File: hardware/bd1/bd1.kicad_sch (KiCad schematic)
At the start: 61 parts, among them J1 Conn_02x03_Odd_Even, U1 STM32L412CBTx

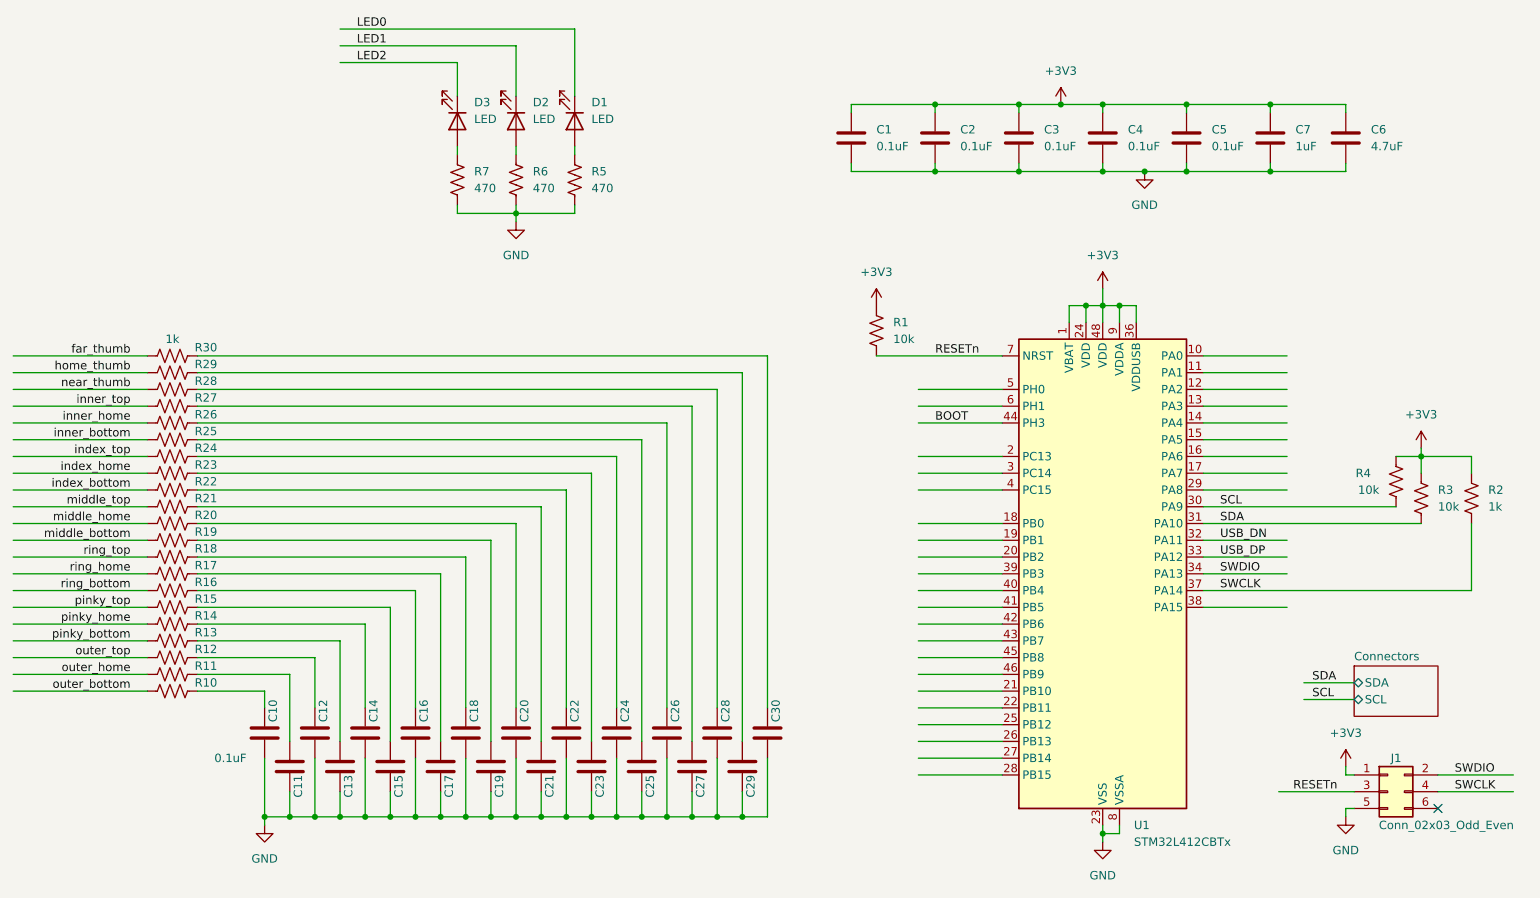
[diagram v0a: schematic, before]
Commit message: USB routing
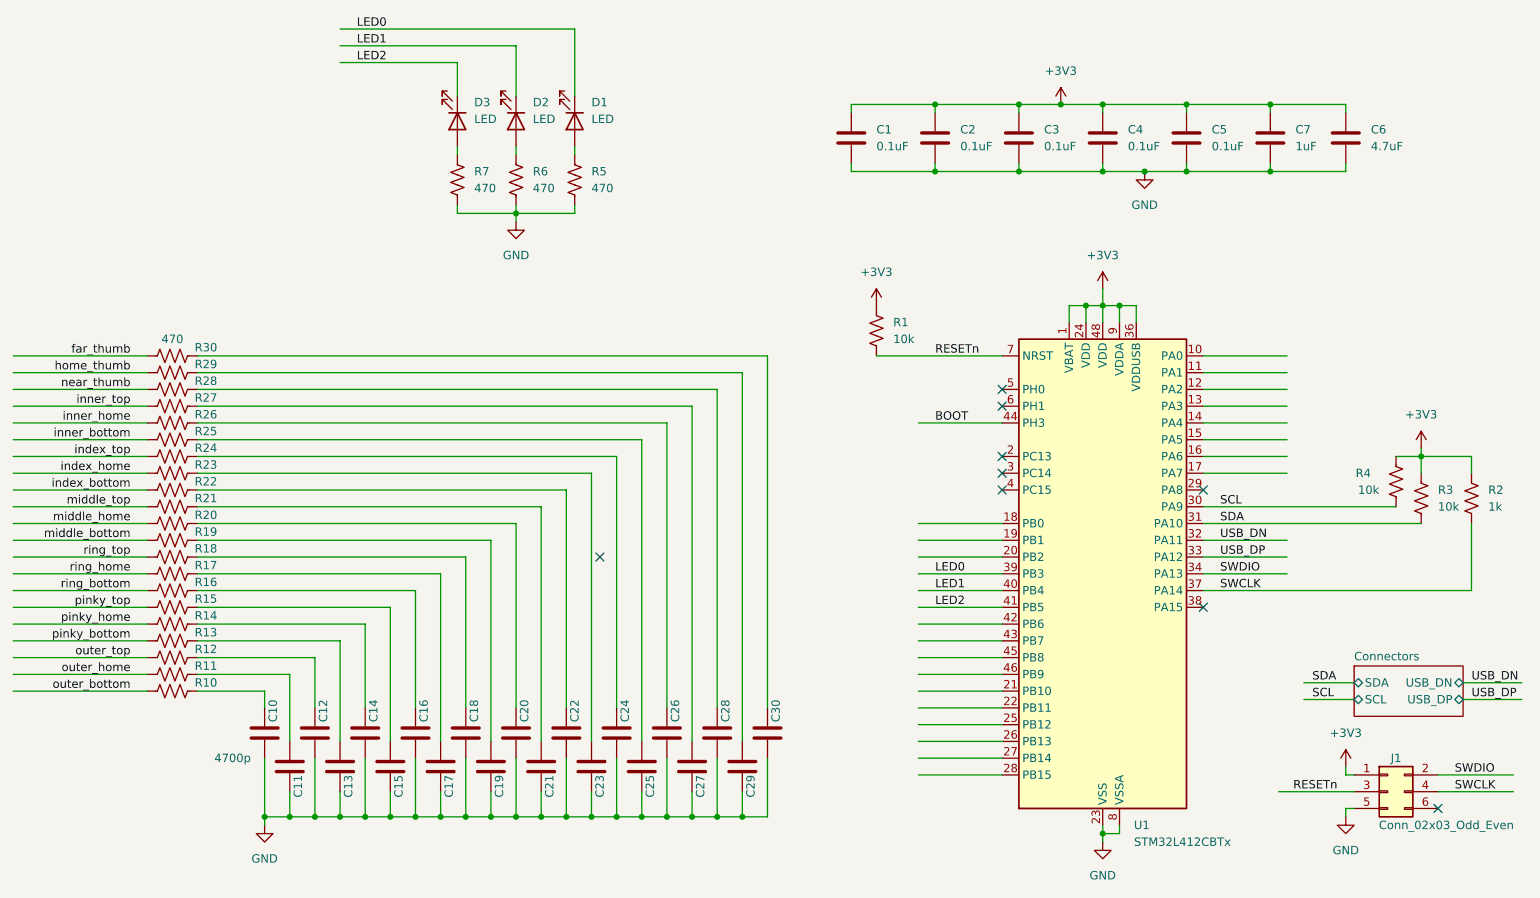
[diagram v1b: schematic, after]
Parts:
- C10, C11, C12, C13, C14, C15, C16, C17, C18, C19, C20, C21, C22, C23, C24, C25, C26, C27, C28, C29, C30: value 0.1uF -> 4700p
- C7: footprint Capacitor_SMD:C_0402_1005Metric -> Capacitor_SMD:C_0603_1608Metric
- R10, R11, R12, R13, R14, R15, R16, R17, R18, R19, R20, R21, R22, R23, R24, R25, R26, R27, R28, R29, R30: value 1k -> 470
- R5, R6, R7: footprint Resistor_SMD:R_0603_1608Metric -> Resistor_SMD:R_0402_1005Metric
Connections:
- net LED0: now also U1.39 (PB3)
- net LED1: now also U1.40 (PB4)
- net LED2: now also U1.41 (PB5)
- no-connect marks 1 -> 9
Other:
- sheet Connectors ports: added USB_DN, USB_DP; removed none

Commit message: Solved routing
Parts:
- C1, C10, C11, C12, C13, C14, C15, C16, C17, C18, C19, C2, C20, C21, C22, C23, C24, C25, C26, C27, C28, C29, C3, C30, C4, C5: footprint Capacitor_SMD:C_0402_1005Metric -> Capacitor_SMD:C_0603_1608Metric
- R10, R11, R12, R13, R14, R15, R16, R17, R18, R19, R2, R20, R21, R22, R23, R24, R25, R26, R27, R28, R29, R30, R5, R6, R7: footprint Resistor_SMD:R_0402_1005Metric -> Resistor_SMD:R_0603_1608Metric
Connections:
- net LED0: now also U1.41 (PB5); no longer U1.39 (PB3)
- net LED2: now also U1.39 (PB3); no longer U1.41 (PB5)
- net PB00: now reaches C13.1, R13.2
- net PB00: now also U1.18 (PB0)
- net PB07: now reaches C26.1, R26.2
- net PB07: now also U1.43 (PB7)
- net PB01: now reaches C14.1, R14.2
- net PB01: now also U1.19 (PB1)
- net PB15: now reaches C30.1, R30.2
- net PB15: now also U1.28 (PB15)
- net PA05: now reaches C16.1, R16.2
- net PA05: now also U1.15 (PA5)
- net PB02: now reaches C15.1, R15.2
- net PB02: now also U1.20 (PB2)
- net PA04: now reaches C21.1, R21.2
- net PA04: now also U1.14 (PA4)
- net PB10: now reaches C10.1, R10.2
- net PB10: now also U1.21 (PB10)
- net PA06: now reaches C17.1, R17.2
- net PA06: now also U1.16 (PA6)
- net PB11: now reaches C11.1, R11.2
- net PB11: now also U1.22 (PB11)
- net PB09: now reaches C22.1, R22.2
- net PB09: now also U1.46 (PB9)
- net PB13: now reaches C28.1, R28.2
- net PB13: now also U1.26 (PB13)
- net PB08: now reaches C27.1, R27.2
- net PB08: now also U1.45 (PB8)
- net PA02: now reaches C19.1, R19.2
- net PA02: now also U1.12 (PA2)
- net PA01: now reaches C24.1, R24.2
- net PA01: now also U1.11 (PA1)
- net PA00: now reaches U1.10 (PA0)
- net PA00: now also C23.1, R23.2
- net PA03: now reaches U1.13 (PA3)
- net PA03: now also C20.1, R20.2
- net PA07: now reaches U1.17 (PA7)
- net PA07: now also C18.1, R18.2
- net PB12: now reaches U1.25 (PB12)
- net PB12: now also C12.1, R12.2
- net PB14: now reaches U1.27 (PB14)
- net PB14: now also C29.1, R29.2
- net PB06: now reaches U1.42 (PB6)
- net PB06: now also C25.1, R25.2
